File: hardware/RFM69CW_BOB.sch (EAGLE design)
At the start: 11 parts, among them U1 RFM69HCW

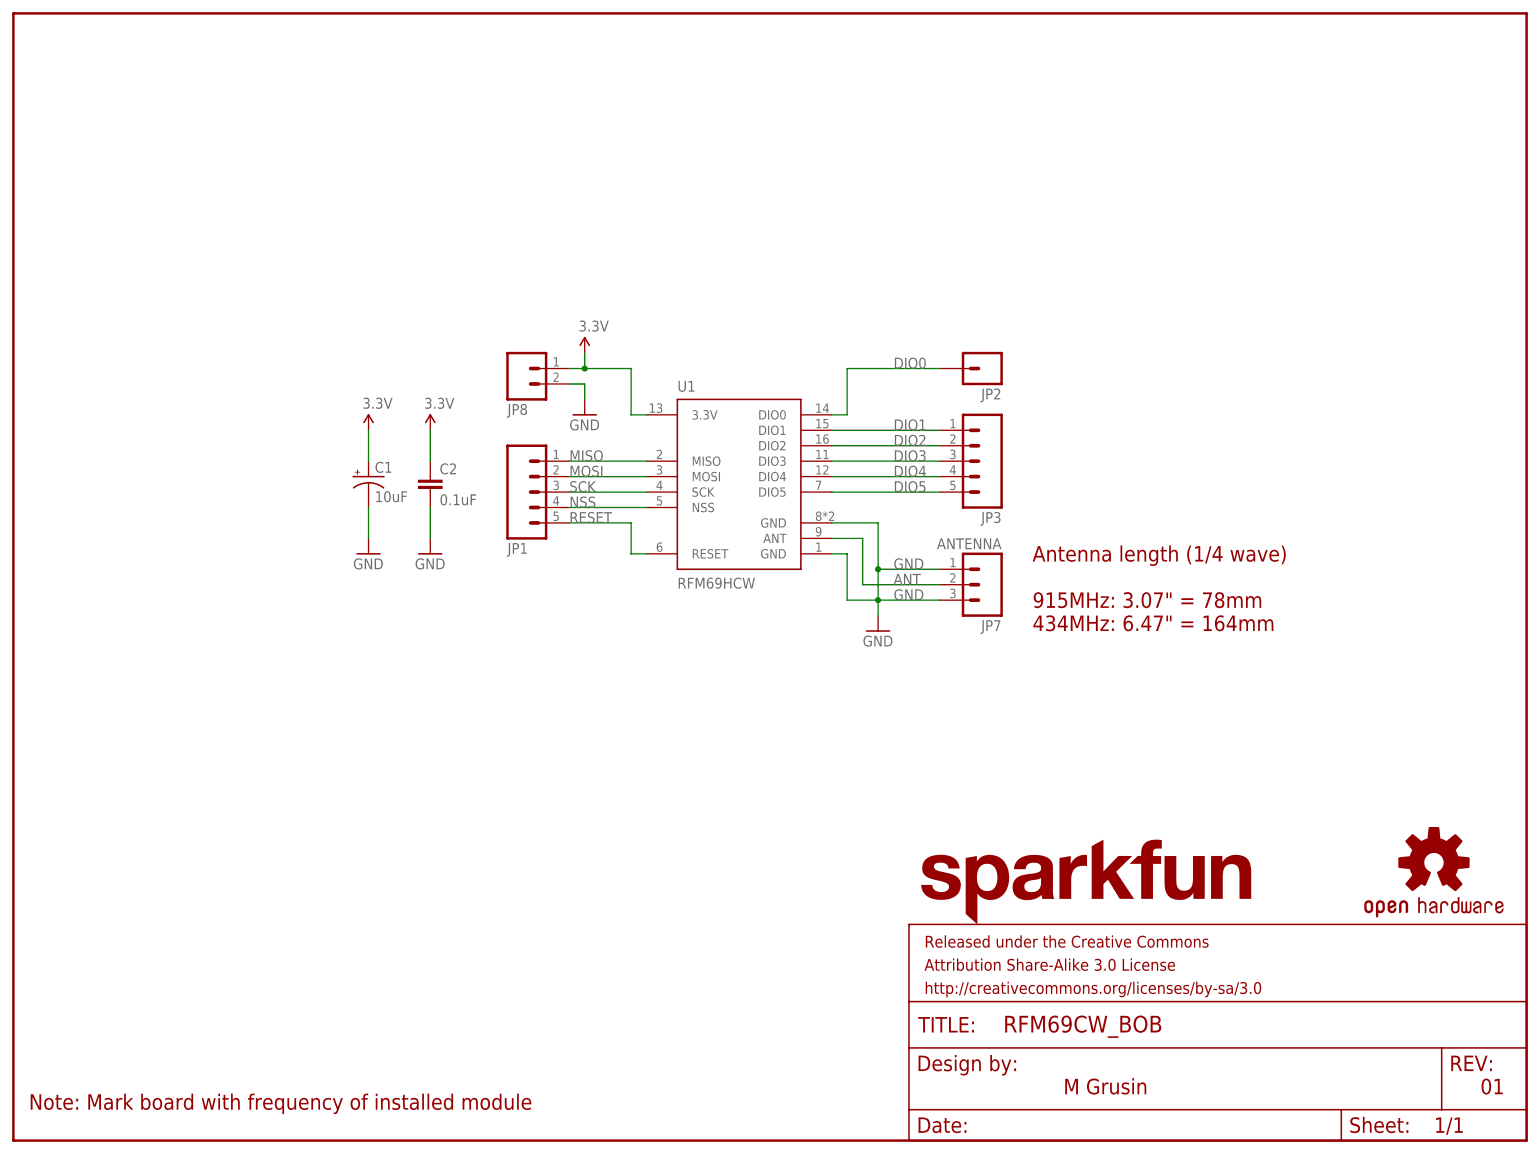
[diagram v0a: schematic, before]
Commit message: HCW BOB to 1.0, CW BOB to 0.1
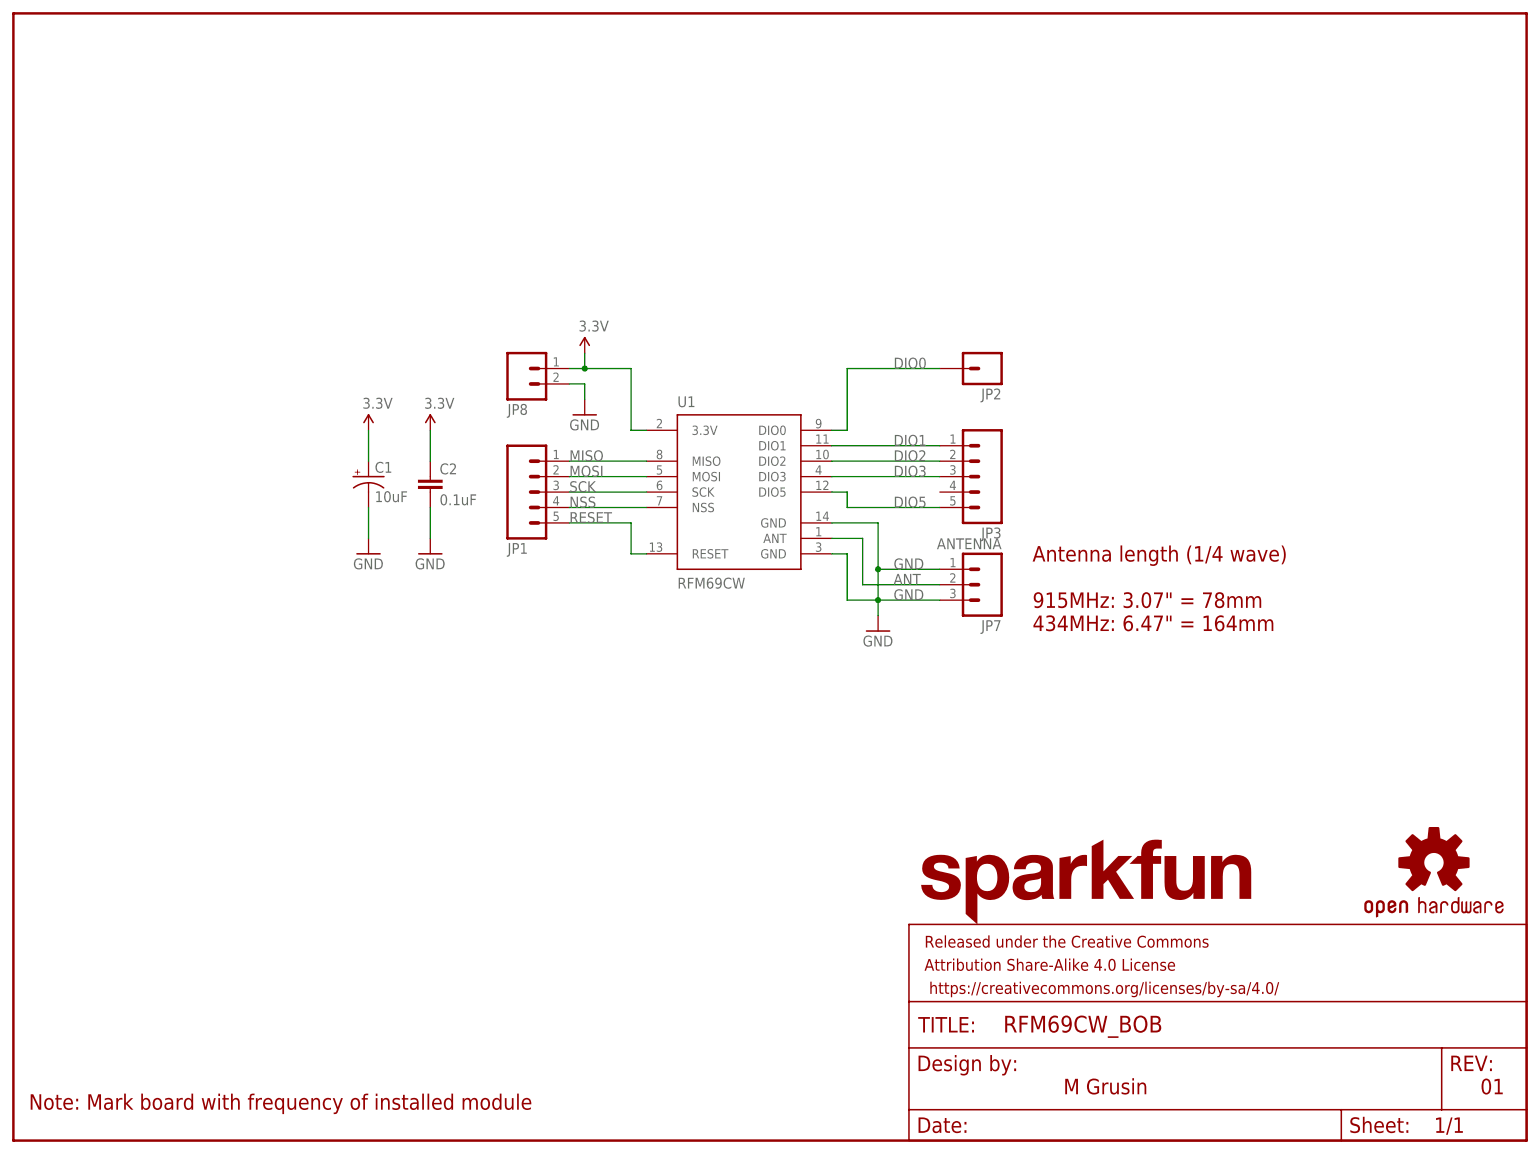
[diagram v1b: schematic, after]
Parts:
- U1: value RFM69HCW -> RFM69CW; device mike-temp:RFM69HCW -> mike-temp:RFM69CW
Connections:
- removed net DIO4: JP3.4, U1.DIO4
- net 3.3V: no longer U1.3.3V
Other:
- moved on the sheet: JP3
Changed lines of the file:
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@@
 </classes>
 <parts>
-<part name="U1" library="mike-temp" deviceset="RFM69H" device="CW" value="RFM69HCW"/>
 <part name="FRAME1" library="SparkFun-Aesthetics" deviceset="FRAME-LETTER" device=""/>
 <part name="C2" library="SparkFun-Capacitors" deviceset="0.1UF-25V(+80/-20%)(0603)" device="" value="0.1uF"/>
@@
 <part name="JP2" library="mike-temp" deviceset="M01" device="SMDNS"/>
 <part name="JP3" library="mike-temp" deviceset="M05" device="_ROUNDONLY_NOSILK"/>
+<part name="U1" library="mike-temp" deviceset="RFM69" device="CW"/>
 </parts>
 <sheets>
@@
 </plain>
 <instances>
-<instance part="U1" gate="G$1" x="119.38" y="106.68"/>
 <instance part="FRAME1" gate="G$1" x="0" y="0"/>
 <instance part="FRAME1" gate="G$2" x="147.32" y="0"/>
@@
 <instance part="JP1" gate="G$1" x="83.82" y="106.68" rot="MR180"/>
 <instance part="JP2" gate="G$1" x="160.02" y="127" rot="R180"/>
-<instance part="JP3" gate="G$1" x="160.02" y="111.76" rot="R180"/>
+<instance part="JP3" gate="G$1" x="160.02" y="109.22" rot="R180"/>
+<instance part="U1" gate="G$1" x="119.38" y="106.68"/>
 </instances>
 <busses>
@@
 <net name="GND" class="0">
 <segment>
-<pinref part="U1" gate="G$1" pin="GND@2"/>
 <pinref part="GND3" gate="1" pin="GND"/>
-<pinref part="U1" gate="G$1" pin="GND@1"/>
 <wire x1="137.16" y1="96.52" x2="137.16" y2="88.9" width="0.1524" layer="91"/>
 <wire x1="134.62" y1="96.52" x2="137.16" y2="96.52" width="0.1524" layer="91"/>
@@
 <wire x1="142.24" y1="88.9" x2="142.24" y2="93.98" width="0.1524" layer="91"/>
 <junction x="142.24" y="93.98"/>
+<pinref part="U1" gate="G$1" pin="GND@1"/>
+<pinref part="U1" gate="G$1" pin="GND@2"/>
 </segment>
 <segment>
@@
 <wire x1="93.98" y1="127" x2="93.98" y2="129.54" width="0.1524" layer="91"/>
 <pinref part="SUPPLY4" gate="G$1" pin="3.3V"/>
-<pinref part="U1" gate="G$1" pin="3.3V"/>
-<wire x1="104.14" y1="119.38" x2="101.6" y2="119.38" width="0.1524" layer="91"/>
-<wire x1="101.6" y1="119.38" x2="101.6" y2="127" width="0.1524" layer="91"/>
+<wire x1="104.14" y1="116.84" x2="101.6" y2="116.84" width="0.1524" layer="91"/>
+<wire x1="101.6" y1="116.84" x2="101.6" y2="127" width="0.1524" layer="91"/>
 <wire x1="101.6" y1="127" x2="93.98" y2="127" width="0.1524" layer="91"/>
 <junction x="93.98" y="127"/>
@@
 <net name="DIO0" class="0">
 <segment>
-<pinref part="U1" gate="G$1" pin="DIO0"/>
 <wire x1="152.4" y1="127" x2="137.16" y2="127" width="0.1524" layer="91"/>
-<wire x1="137.16" y1="127" x2="137.16" y2="119.38" width="0.1524" layer="91"/>
-<wire x1="137.16" y1="119.38" x2="134.62" y2="119.38" width="0.1524" layer="91"/>
+<wire x1="137.16" y1="127" x2="137.16" y2="116.84" width="0.1524" layer="91"/>
 <label x="144.78" y="127" size="1.778" layer="95"/>
 <pinref part="JP2" gate="G$1" pin="1"/>
-</segment>
-</net>
-<net name="DIO1" class="0">
-<segment>
-<pinref part="U1" gate="G$1" pin="DIO1"/>
-<wire x1="152.4" y1="116.84" x2="134.62" y2="116.84" width="0.1524" layer="91"/>
-<label x="144.78" y="116.84" size="1.778" layer="95"/>
-<pinref part="JP3" gate="G$1" pin="1"/>
-</segment>
-</net>
-<net name="DIO2" class="0">
-<segment>
-<pinref part="U1" gate="G$1" pin="DIO2"/>
-<wire x1="152.4" y1="114.3" x2="134.62" y2="114.3" width="0.1524" layer="91"/>
-<label x="144.78" y="114.3" size="1.778" layer="95"/>
-<pinref part="JP3" gate="G$1" pin="2"/>
-</segment>
-</net>
-<net name="DIO3" class="0">
-<segment>
-<pinref part="U1" gate="G$1" pin="DIO3"/>
-<wire x1="152.4" y1="111.76" x2="134.62" y2="111.76" width="0.1524" layer="91"/>
-<label x="144.78" y="111.76" size="1.778" layer="95"/>
-<pinref part="JP3" gate="G$1" pin="3"/>
+<pinref part="U1" gate="G$1" pin="DIO0"/>
+<wire x1="134.62" y1="116.84" x2="137.16" y2="116.84" width="0.1524" layer="91"/>
 </segment>
 </net>
 <net name="MISO" class="0">
 <segment>
-<pinref part="U1" gate="G$1" pin="MISO"/>
 <wire x1="91.44" y1="111.76" x2="104.14" y2="111.76" width="0.1524" layer="91"/>
 <label x="91.44" y="111.76" size="1.778" layer="95"/>
 <pinref part="JP1" gate="G$1" pin="1"/>
+<pinref part="U1" gate="G$1" pin="MISO"/>
 </segment>
 </net>
 <net name="MOSI" class="0">
 <segment>
-<pinref part="U1" gate="G$1" pin="MOSI"/>
 <wire x1="91.44" y1="109.22" x2="104.14" y2="109.22" width="0.1524" layer="91"/>
 <label x="91.44" y="109.22" size="1.778" layer="95"/>
 <pinref part="JP1" gate="G$1" pin="2"/>
+<pinref part="U1" gate="G$1" pin="MOSI"/>
 </segment>
 </net>
 <net name="SCK" class="0">
 <segment>
-<pinref part="U1" gate="G$1" pin="SCK"/>
 <wire x1="91.44" y1="106.68" x2="104.14" y2="106.68" width="0.1524" layer="91"/>
 <label x="91.44" y="106.68" size="1.778" layer="95"/>
 <pinref part="JP1" gate="G$1" pin="3"/>
+<pinref part="U1" gate="G$1" pin="SCK"/>
 </segment>
 </net>
 <net name="NSS" class="0">
 <segment>
-<pinref part="U1" gate="G$1" pin="NSS"/>
 <wire x1="91.44" y1="104.14" x2="104.14" y2="104.14" width="0.1524" layer="91"/>
 <label x="91.44" y="104.14" size="1.778" layer="95"/>
 <pinref part="JP1" gate="G$1" pin="4"/>
+<pinref part="U1" gate="G$1" pin="NSS"/>
 </segment>
 </net>
 <net name="RESET" class="0">
 <segment>
-<pinref part="U1" gate="G$1" pin="RESET"/>
 <wire x1="101.6" y1="96.52" x2="104.14" y2="96.52" width="0.1524" layer="91"/>
 <label x="91.44" y="101.6" size="1.778" layer="95"/>
@@
 <wire x1="91.44" y1="101.6" x2="101.6" y2="101.6" width="0.1524" layer="91"/>
 <wire x1="101.6" y1="101.6" x2="101.6" y2="96.52" width="0.1524" layer="91"/>
+<pinref part="U1" gate="G$1" pin="RESET"/>
 </segment>
 </net>
@@
 <segment>
 <pinref part="JP7" gate="G$1" pin="2"/>
-<pinref part="U1" gate="G$1" pin="ANT"/>
 <wire x1="152.4" y1="91.44" x2="139.7" y2="91.44" width="0.1524" layer="91"/>
 <wire x1="139.7" y1="91.44" x2="139.7" y2="99.06" width="0.1524" layer="91"/>
 <wire x1="139.7" y1="99.06" x2="134.62" y2="99.06" width="0.1524" layer="91"/>
 <label x="144.78" y="91.44" size="1.778" layer="95"/>
+<pinref part="U1" gate="G$1" pin="ANT"/>
 </segment>
 </net>
 <net name="DIO5" class="0">
 <segment>
+<wire x1="134.62" y1="106.68" x2="137.16" y2="106.68" width="0.1524" layer="91"/>
+<wire x1="137.16" y1="106.68" x2="137.16" y2="104.14" width="0.1524" layer="91"/>
+<wire x1="137.16" y1="104.14" x2="152.4" y2="104.14" width="0.1524" layer="91"/>
+<label x="144.78" y="104.14" size="1.778" layer="95"/>
+<pinref part="JP3" gate="G$1" pin="5"/>
 <pinref part="U1" gate="G$1" pin="DIO5"/>
-<wire x1="134.62" y1="106.68" x2="152.4" y2="106.68" width="0.1524" layer="91"/>
-<label x="144.78" y="106.68" size="1.778" layer="95"/>
-<pinref part="JP3" gate="G$1" pin="5"/>
-</segment>
-</net>
-<net name="DIO4" class="0">
-<segment>
-<pinref part="U1" gate="G$1" pin="DIO4"/>
-<wire x1="152.4" y1="109.22" x2="134.62" y2="109.22" width="0.1524" layer="91"/>
+</segment>
+</net>
+<net name="DIO3" class="0">
+<segment>
+<pinref part="U1" gate="G$1" pin="DIO3"/>
+<pinref part="JP3" gate="G$1" pin="3"/>
+<wire x1="134.62" y1="109.22" x2="152.4" y2="109.22" width="0.1524" layer="91"/>
 <label x="144.78" y="109.22" size="1.778" layer="95"/>
-<pinref part="JP3" gate="G$1" pin="4"/>
-</segment>
-</net>
+</segment>
+</net>
+<net name="DIO2" class="0">
+<segment>
+<pinref part="JP3" gate="G$1" pin="2"/>
+<pinref part="U1" gate="G$1" pin="DIO2"/>
+<wire x1="152.4" y1="111.76" x2="134.62" y2="111.76" width="0.1524" layer="91"/>
+<label x="144.78" y="111.76" size="1.778" layer="95"/>
+</segment>
+</net>
+<net name="DIO1" class="0">
+<segment>
+<pinref part="U1" gate="G$1" pin="DIO1"/>
+<pinref part="JP3" gate="G$1" pin="1"/>
+<wire x1="134.62" y1="114.3" x2="152.4" y2="114.3" width="0.1524" layer="91"/>
+<label x="144.78" y="114.3" size="1.778" layer="95"/>
+</segment>
+</net>
